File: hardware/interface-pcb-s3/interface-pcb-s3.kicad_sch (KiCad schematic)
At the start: 11 parts, among them SW1 setup, U5 ESP32 D1 Mini

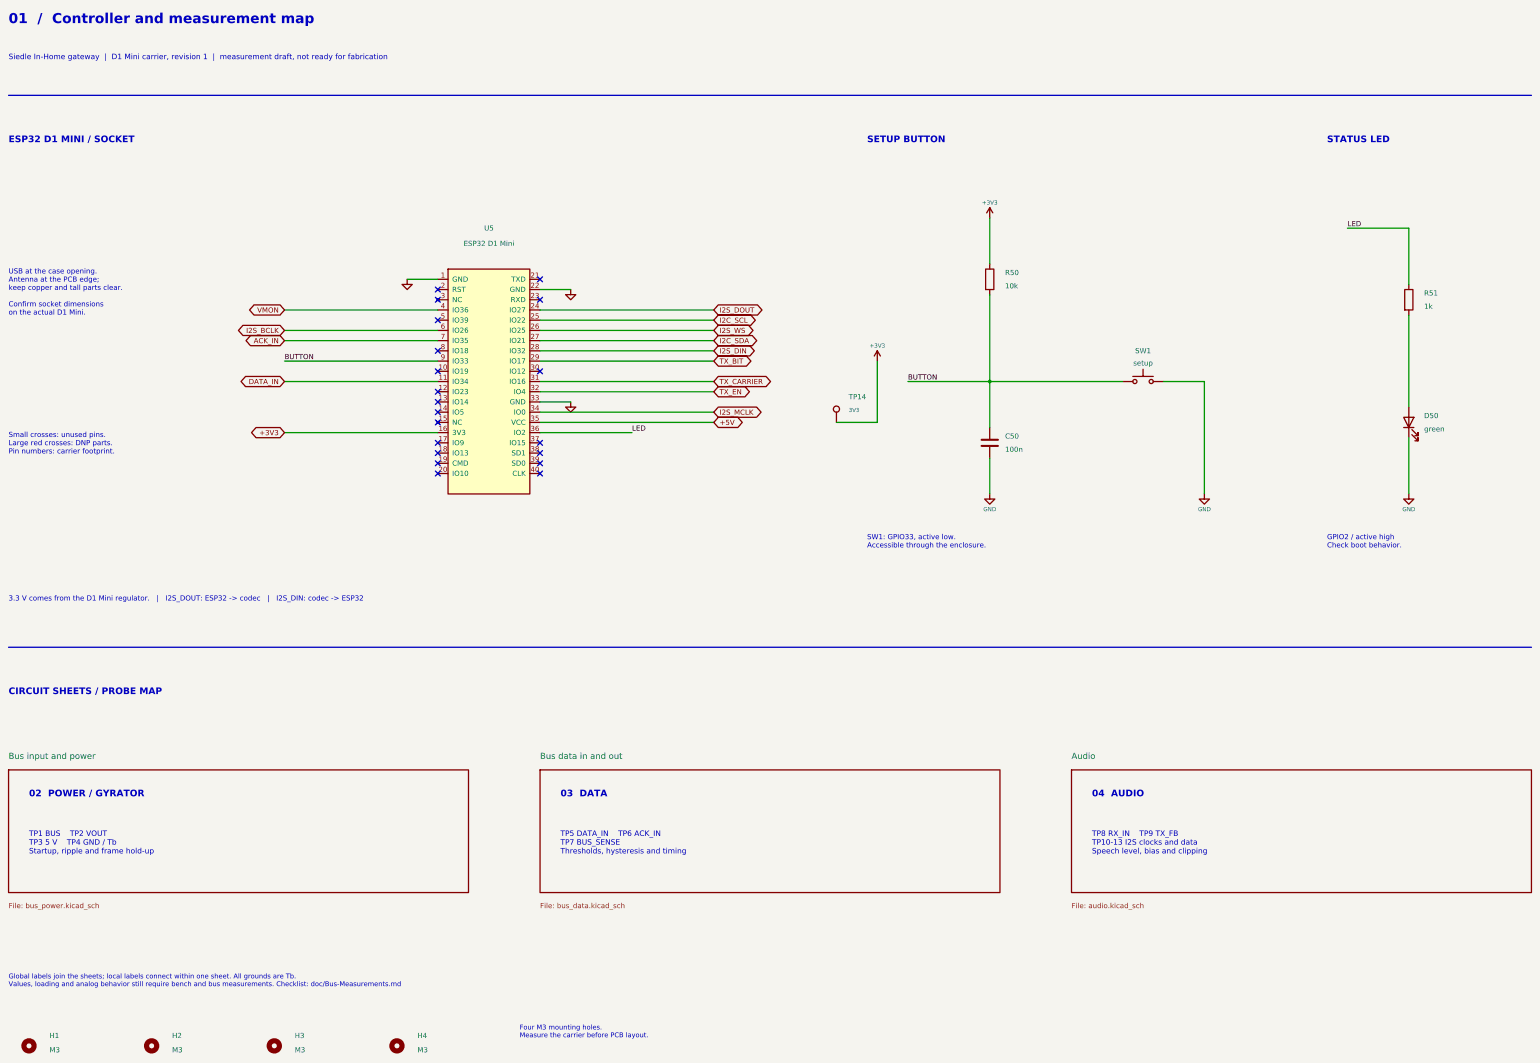
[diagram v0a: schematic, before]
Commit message: Put an ESP32-S3 module on the board and run it on 3.3 V
The S3 variant replaces the plug-in D1 Mini with an ESP32-S3-WROOM-1-
N16R8 that JLCPCB places (C2913202). That saves the second board
revision that was planned for a module, and the 8 MB PSRAM runs ESP-SR's
echo cancellation for full duplex.

Without the D1 Mini nothing needs 5 V: U1 becomes the R-78CK3.3-0.5 and
feeds the module, the codec, the comparators and the op-amp directly,
instead of losing a third in the D1 Mini's linear regulator. JP1 goes;
D2 now feeds the unfitted J2 (9-24 V) into VOUT ahead of U1, where the
gyrator steps back by itself.

The controller sheet gets the module with its decoupling and power-on
reset (EN 10 k / 1 uF, SW2), USB-C on the S3's native USB for flashing
and logs (USBLC6 ESD protection, 5.1 k CC pull-downs, VBUS not used for
power), UART0 test points, and SW1 moves to GPIO0, the BOOT pin the
firmware already uses for the setup hotspot. PCB-S3.md has the pin plan
and the differences against the D1 Mini variant.

ERC: no violations. Compared with the D1 Mini variant's netlist, only
the supply, the module and the new parts changed. The layout still
shows the D1 Mini; it follows after the review.

Co-Authored-By: Claude Opus 5.5 <noreply@anthropic.com>
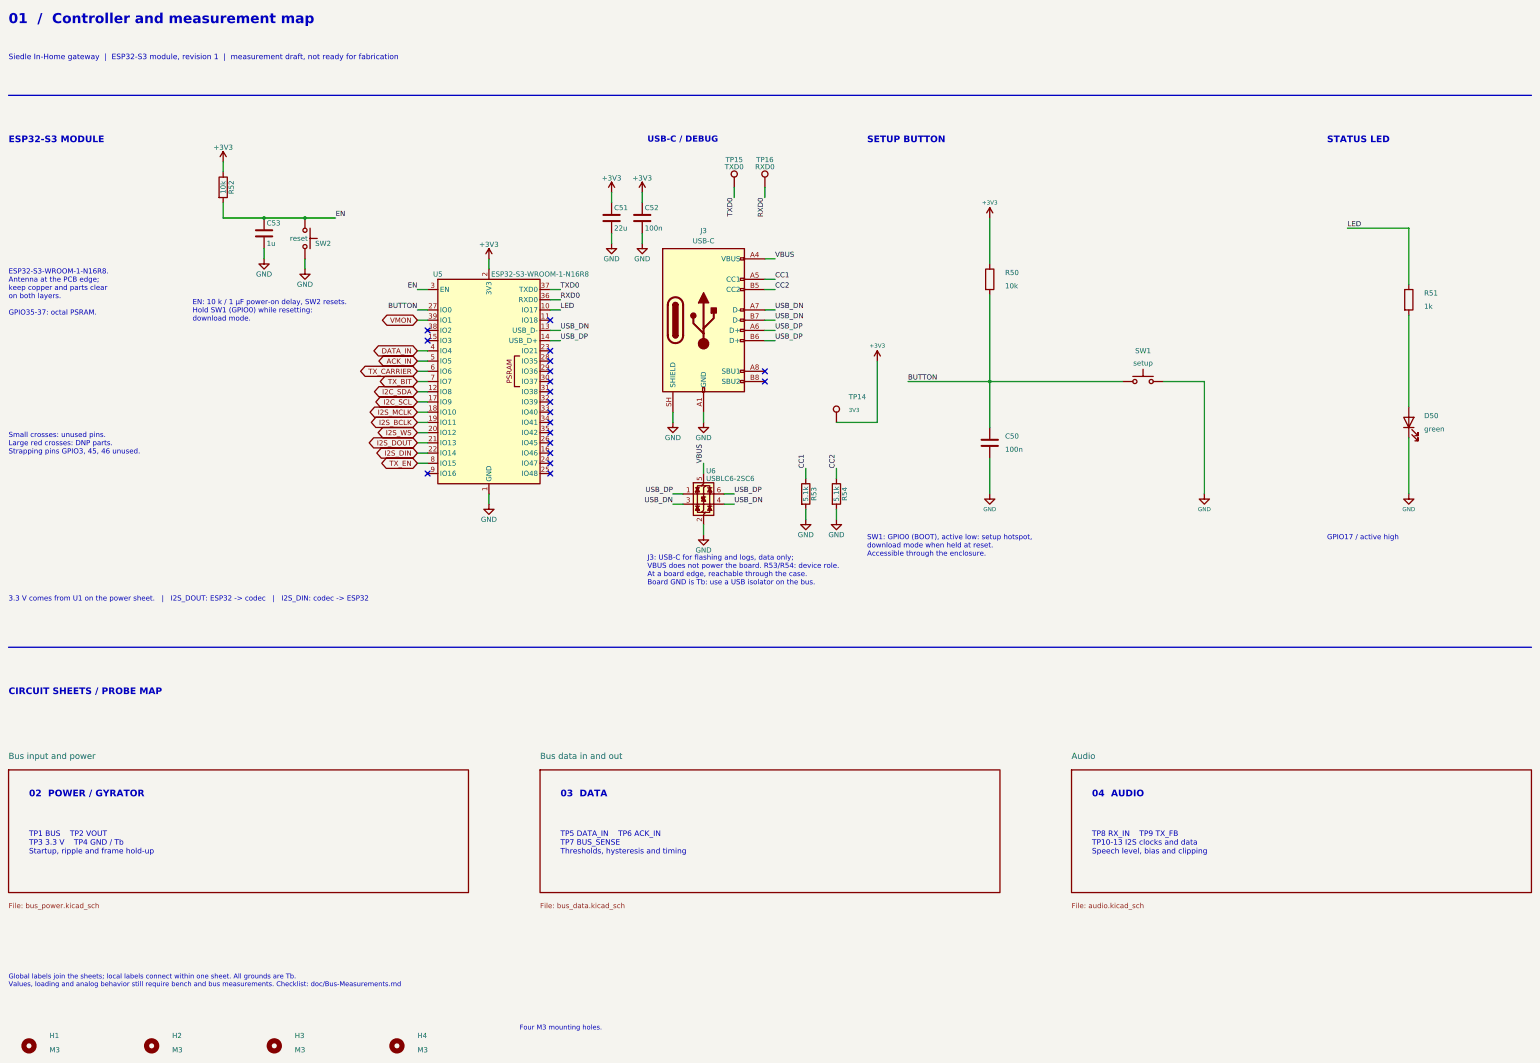
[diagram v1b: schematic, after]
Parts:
- removed U5: ESP32 D1 Mini, gateway:D1_Mini_ESP32_Socket, symbol gateway:D1_Mini_ESP32
- added C51: 22u, Capacitor_SMD:C_0805_2012Metric, symbol Device:C
- added C52: 100n, Capacitor_SMD:C_0805_2012Metric, symbol Device:C
- added C53: 1u, Capacitor_SMD:C_0805_2012Metric, symbol Device:C
- added J3: USB-C, Connector_USB:USB_C_Receptacle_HRO_TYPE-C-31-M-12, symbol Connector:USB_C_Receptacle_USB2.0_16P
- added R52: 10k, Resistor_SMD:R_0805_2012Metric, symbol Device:R
- added R53, R54: 5.1k, Resistor_SMD:R_0805_2012Metric, symbol Device:R
- added SW2: reset, Button_Switch_SMD:SW_Push_1P1T_XKB_TS-1187A, symbol Switch:SW_Push
- added TP15: TXD0, TestPoint:TestPoint_Pad_D1.5mm, symbol Connector:TestPoint
- added TP16: RXD0, TestPoint:TestPoint_Pad_D1.5mm, symbol Connector:TestPoint
- added U5: ESP32-S3-WROOM-1-N16R8, RF_Module:ESP32-S3-WROOM-1, symbol RF_Module:ESP32-S3-WROOM-1
- added U6: USBLC6-2SC6, Package_TO_SOT_SMD:SOT-23-6, symbol Power_Protection:USBLC6-2SC6
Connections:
- net +3V3: now also C51.1, C52.1, R52.1, U5.2 (3V3)
- net ACK_IN: now also U5.5 (IO5)
- net BUTTON: now also U5.27 (IO0)
- net DATA_IN: now also U5.4 (IO4)
- net GND: now also C51.2, C52.2, C53.2, J3.A1 (GND), J3.A12 (GND), J3.B1 (GND), J3.B12 (GND), J3.SH (SHIELD), R53.2, R54.2, SW2.2, U5.1 (GND), U5.40 (GND), U5.41 (GND), U6.2 (GND)
- net I2C_SCL: now also U5.17 (IO9)
- net I2C_SDA: now also U5.12 (IO8)
- net I2S_BCLK: now also U5.19 (IO11)
- net I2S_DIN: now also U5.22 (IO14)
- net I2S_DOUT: now also U5.21 (IO13)
- net I2S_MCLK: now also U5.18 (IO10)
- net I2S_WS: now also U5.20 (IO12)
- net LED: now also U5.10 (IO17)
- net TX_BIT: now also U5.7 (IO7)
- net TX_CARRIER: now also U5.6 (IO6)
- net TX_EN: now also U5.8 (IO15)
- net VMON: now also U5.39 (IO1)
- new net CC1: J3.A5 (CC1), R53.1
- new net CC2: J3.B5 (CC2), R54.1
- new net EN: C53.1, R52.2, SW2.1, U5.3 (EN)
- new net RXD0: TP16.1, U5.36 (RXD0)
- new net TXD0: TP15.1, U5.37 (TXD0)
- new net USB_DN: J3.A7 (D-), J3.B7 (D-), U5.13 (USB_D-), U6.3 (I/O2), U6.4 (I/O2)
- new net USB_DP: J3.A6 (D+), J3.B6 (D+), U5.14 (USB_D+), U6.1 (I/O1), U6.6 (I/O1)
- new net VBUS: J3.A4 (VBUS), J3.A9 (VBUS), J3.B4 (VBUS), J3.B9 (VBUS), U6.5 (VBUS)
- no-connect marks 20 -> 19
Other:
- note added: "3.3 V comes from U1 on the power sheet. | I2S_DOUT: ESP32 -> codec | I2S_DIN: codec -> ESP32"
- note added: "EN: 10 k / 1 µF power-on delay, SW2 resets. Hold SW1 (GPIO0) while resetting: download mode."
- note added: "ESP32-S3 MODULE"
- note added: "ESP32-S3-WROOM-1-N16R8. Antenna at the PCB edge; keep copper and parts clear on both layers. GPIO35-37: octal PSRAM."
- note added: "Four M3 mounting holes."
- note added: "GPIO17 / active high"
- note added: "J3: USB-C for flashing and logs, data only; VBUS does not power the board. R53/R54: device role. At a board edge, reachable through the case. Board GND is Tb: use a USB isolator on the bus."
- note added: "SW1: GPIO0 (BOOT), active low: setup hotspot, download mode when held at reset. Accessible through the enclosure."
- note added: "Siedle In-Home gateway | ESP32-S3 module, revision 1 | measurement draft, not ready for fabrication"
- note added: "Small crosses: unused pins. Large red crosses: DNP parts. Strapping pins GPIO3, 45, 46 unused."
- note added: "TP1 BUS TP2 VOUT TP3 3.3 V TP4 GND / Tb Startup, ripple and frame hold-up"
- note added: "USB-C / DEBUG"
- note removed: "3.3 V comes from the D1 Mini regulator. | I2S_DOUT: ESP32 -> codec | I2S_DIN: codec -> ESP32"
- note removed: "ESP32 D1 MINI / SOCKET"
- note removed: "Four M3 mounting holes. Measure the carrier before PCB layout."
- note removed: "GPIO2 / active high Check boot behavior."
- note removed: "SW1: GPIO33, active low. Accessible through the enclosure."
- note removed: "Siedle In-Home gateway | D1 Mini carrier, revision 1 | measurement draft, not ready for fabrication"
- note removed: "Small crosses: unused pins. Large red crosses: DNP parts. Pin numbers: carrier footprint."
- note removed: "TP1 BUS TP2 VOUT TP3 5 V TP4 GND / Tb Startup, ripple and frame hold-up"
- note removed: "USB at the case opening. Antenna at the PCB edge; keep copper and tall parts clear. Confirm socket dimensions on the actual D1 Mini."

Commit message: Group the module's pins by the side they leave on
The VOUT monitor sat on IO1 and the LED on IO17, on the module sides
facing away from their circuits: VMON would have crossed under the
module to reach the bus side, and the LED line ran between the data
signals. VMON moves to IO7 (also ADC1) and TX_BIT to the free IO16, so
all bus and supply pins leave on the module's left side; the LED moves
to IO38, next to the button on the right side.

Co-Authored-By: Claude Opus 5.5 <noreply@anthropic.com>
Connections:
- net LED: now also U5.31 (IO38); no longer U5.10 (IO17)
- net TX_BIT: now also U5.9 (IO16); no longer U5.7 (IO7)
- net VMON: now also U5.7 (IO7); no longer U5.39 (IO1)
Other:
- note added: "GPIO38 / active high"
- note removed: "GPIO17 / active high"
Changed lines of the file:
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@@
 		)
 	)
-	(wire
-		(pts
-			(xy 121.92 96.52) (xy 119.38 96.52)
-		)
-		(stroke
-			(width 0)
-			(type default)
-		)
-	)
-	(global_label "VMON"
-		(shape bidirectional)
-		(at 119.38 96.52 180)
-		(fields_autoplaced yes)
-		(effects
-			(font
-				(size 1.27 1.27)
-			)
-			(justify right)
-		)
-		(property "Intersheetrefs" "${INTERSHEET_REFS}"
-			(at 119.38 96.52 0)
-			(effects
-				(font
-					(size 1.27 1.27)
-				)
-				(justify right)
-				(hide yes)
-			)
-		)
-	)
 	(no_connect
 		(at 121.92 99.06)
@@
 		)
 	)
-	(global_label "TX_BIT"
+	(global_label "VMON"
 		(shape bidirectional)
 		(at 119.38 111.76 180)
@@
 		)
 	)
-	(no_connect
-		(at 121.92 134.62)
-	)
 	(wire
 		(pts
@@
 		)
 	)
-	(wire
-		(pts
-			(xy 152.4 93.98) (xy 154.94 93.98)
-		)
-		(stroke
-			(width 0)
-			(type default)
-		)
-	)
-	(label "LED"
-		(at 154.94 93.98 0)
-		(effects
-			(font
-				(size 1.27 1.27)
-			)
-			(justify left bottom)
-		)
-	)
 	(no_connect
 		(at 152.4 96.52)
@@
 	)
 	(no_connect
-		(at 152.4 114.3)
-	)
-	(no_connect
 		(at 152.4 116.84)
 	)
@@
 		)
 	)
+	(no_connect
+		(at 121.92 96.52)
+	)
+	(wire
+		(pts
+			(xy 121.92 134.62) (xy 119.38 134.62)
+		)
+		(stroke
+			(width 0)
+			(type default)
+		)
+	)
+	(global_label "TX_BIT"
+		(shape bidirectional)
+		(at 119.38 134.62 180)
+		(fields_autoplaced yes)
+		(effects
+			(font
+				(size 1.27 1.27)
+			)
+			(justify right)
+		)
+		(property "Intersheetrefs" "${INTERSHEET_REFS}"
+			(at 119.38 134.62 0)
+			(effects
+				(font
+					(size 1.27 1.27)
+				)
+				(justify right)
+				(hide yes)
+			)
+		)
+	)
+	(no_connect
+		(at 152.4 93.98)
+	)
+	(wire
+		(pts
+			(xy 152.4 114.3) (xy 154.94 114.3)
+		)
+		(stroke
+			(width 0)
+			(type default)
+		)
+	)
+	(label "LED"
+		(at 154.94 114.3 0)
+		(effects
+			(font
+				(size 1.27 1.27)
+			)
+			(justify left bottom)
+		)
+	)
 	(sheet_instances
 		(path "/"
@@
 		)
 	)
-	(text "GPIO17 / active high"
+	(text "GPIO38 / active high"
 		(exclude_from_sim no)
 		(at 345.44 149.86 0)

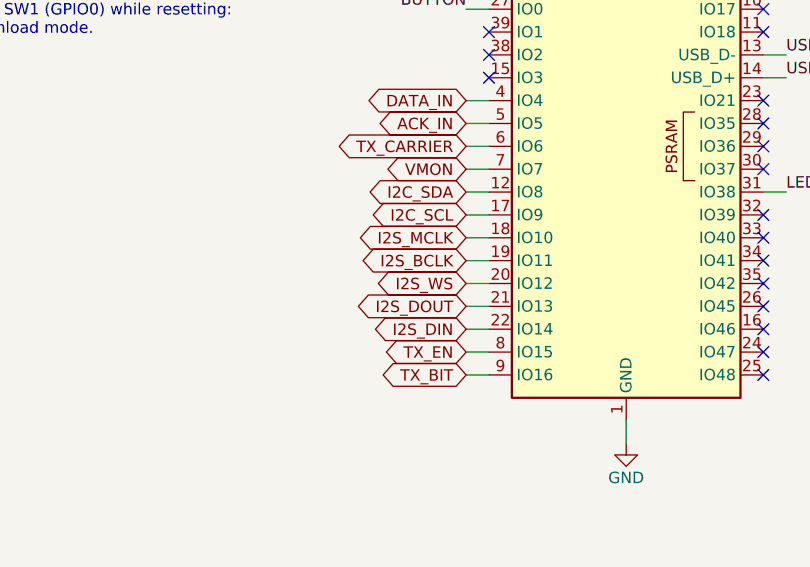
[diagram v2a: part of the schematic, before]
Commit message: Order the I2S pins along the module as the codec needs them
The module's bottom row now carries DOUT, WS, DIN, BCLK and MCLK on
GPIO10-14, the order in which the codec's pins take them. The I2S lines
then run from the module to the codec side by side without crossing,
and MCLK ends at its series resistor. The S3 routes I2S to any GPIO, so
this only changes the pin plan.

Co-Authored-By: Claude Opus 5.5 <noreply@anthropic.com>
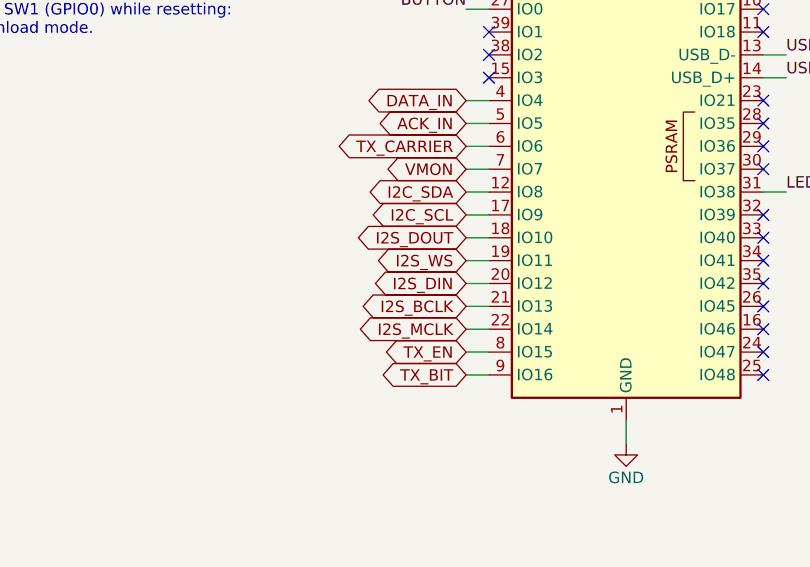
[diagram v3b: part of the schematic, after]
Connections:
- net I2S_BCLK: now also U5.21 (IO13); no longer U5.19 (IO11)
- net I2S_DIN: now also U5.20 (IO12); no longer U5.22 (IO14)
- net I2S_DOUT: now also U5.18 (IO10); no longer U5.21 (IO13)
- net I2S_MCLK: now also U5.22 (IO14); no longer U5.18 (IO10)
- net I2S_WS: now also U5.19 (IO11); no longer U5.20 (IO12)
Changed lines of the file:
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@@
 		)
 	)
-	(global_label "I2S_MCLK"
+	(global_label "I2S_DOUT"
 		(shape bidirectional)
 		(at 119.38 119.38 180)
@@
 		)
 	)
-	(global_label "I2S_BCLK"
+	(global_label "I2S_WS"
 		(shape bidirectional)
 		(at 119.38 121.92 180)
@@
 		)
 	)
-	(global_label "I2S_WS"
+	(global_label "I2S_DIN"
 		(shape bidirectional)
 		(at 119.38 124.46 180)
@@
 		)
 	)
-	(global_label "I2S_DOUT"
+	(global_label "I2S_BCLK"
 		(shape bidirectional)
 		(at 119.38 127 180)
@@
 		)
 	)
-	(global_label "I2S_DIN"
+	(global_label "I2S_MCLK"
 		(shape bidirectional)
 		(at 119.38 129.54 180)
